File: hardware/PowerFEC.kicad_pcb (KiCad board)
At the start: 2 copper layers, 24 x 27.9 mm, 27 parts, among them J1 105444-0001, J2 B2B-XH-A, U1 PIC16F1455, U2 AP22652, U3 ZXCT1009

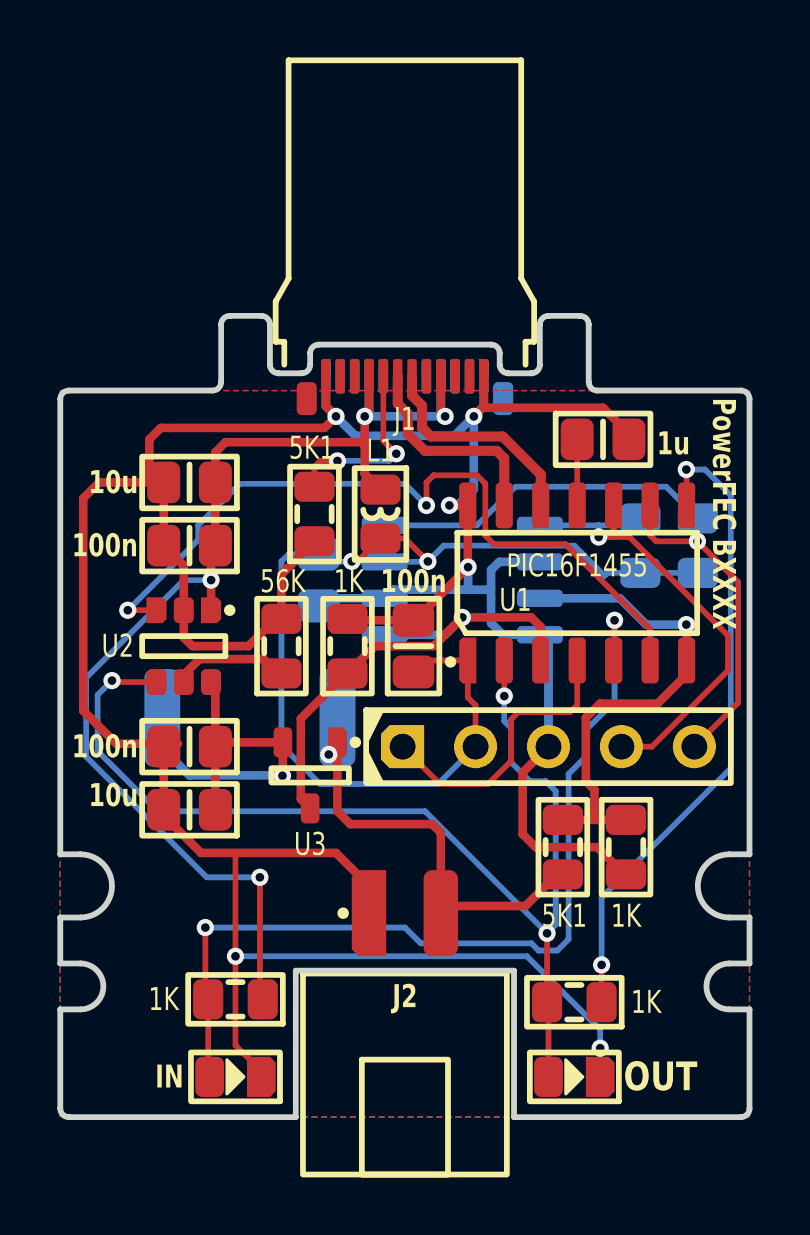
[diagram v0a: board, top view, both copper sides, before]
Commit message: Added 10nF capacitor
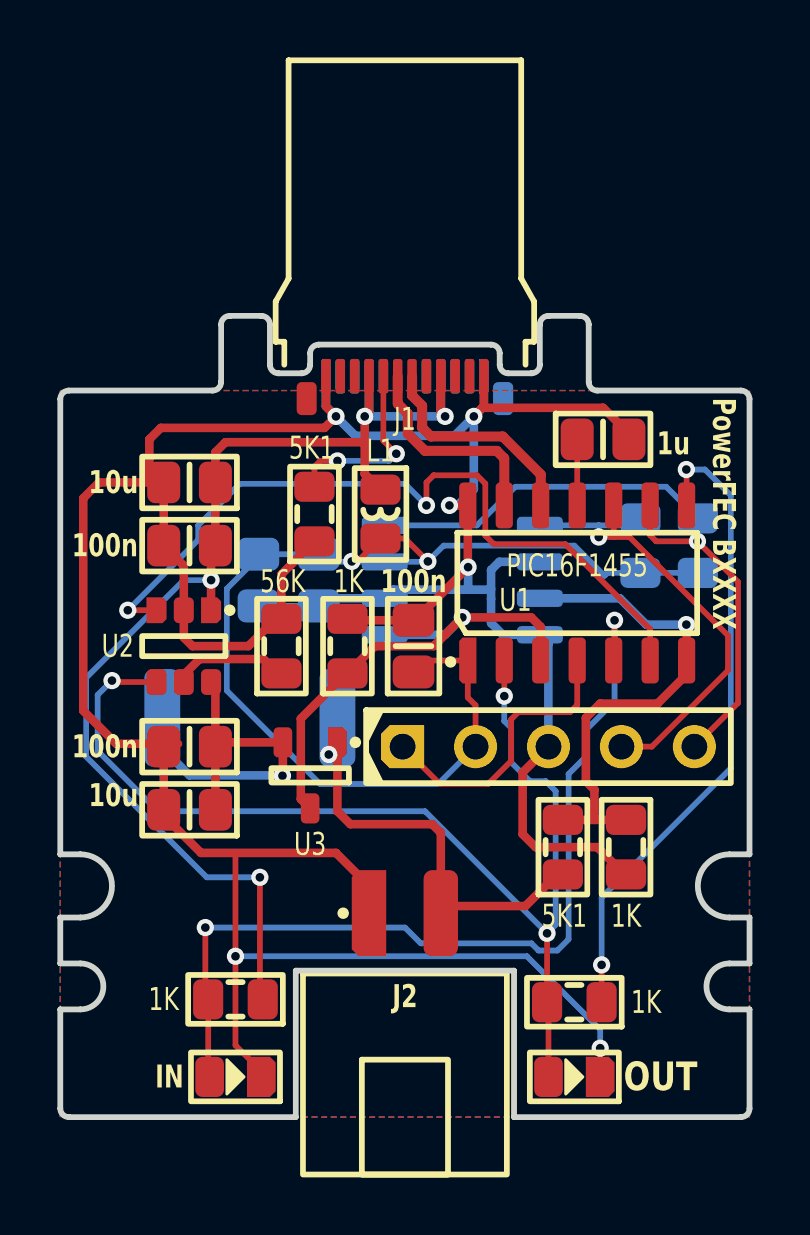
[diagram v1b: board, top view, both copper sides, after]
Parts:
- added C5: 100n, Medo64:C (0805), B.Cu at (26.9, 29.2)
- C1: renamed from C4; value 100n -> 10n
- renumbered C1 to C2, C2 to C3, C3 to C4, C5 to C6, C6 to C7, C7 to C8
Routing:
- net 5V: track 37.4 -> 39.6 mm
- net GND: track 124.7 -> 126.7 mm
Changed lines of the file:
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@@
     (tags "CAPC2013X140N")
     (attr smd)
-    (fp_text reference "C7" (at 0 -1.6) (layer "F.SilkS") hide
+    (fp_text reference "C8" (at 0 -1.6) (layer "F.SilkS") hide
         (effects (font (size 0.8 0.6) (thickness 0.15) bold))
     )
@@
     (tags "CAPC2013X140N")
     (attr smd)
-    (fp_text reference "C6" (at 0 -1.6) (layer "F.SilkS") hide
+    (fp_text reference "C7" (at 0 -1.6) (layer "F.SilkS") hide
         (effects (font (size 0.8 0.6) (thickness 0.15) bold))
     )
@@
     (tags "CAPC2013X140N")
     (attr smd)
-    (fp_text reference "C1" (at 0 -1.6) (layer "F.SilkS") hide
+    (fp_text reference "C2" (at 0 -1.6) (layer "F.SilkS") hide
         (effects (font (size 0.8 0.6) (thickness 0.15) bold))
     )
@@
     (tags "CAPC2013X140N")
     (attr smd)
-    (fp_text reference "C2" (at 0 -1.6) (layer "F.SilkS") hide
+    (fp_text reference "C3" (at 0 -1.6) (layer "F.SilkS") hide
         (effects (font (size 0.8 0.6) (thickness 0.15) bold))
     )
@@
     (tags "CAPC2013X140N")
     (attr smd)
-    (fp_text reference "C5" (at 0 -1.6) (layer "F.SilkS") hide
+    (fp_text reference "C6" (at 0 -1.6) (layer "F.SilkS") hide
         (effects (font (size 0.8 0.6) (thickness 0.15) bold))
     )
@@
     (tags "CAPC2013X140N")
     (attr smd)
-    (fp_text reference "C3" (at 0 -1.6 90) (layer "F.SilkS") hide
+    (fp_text reference "C4" (at 0 -1.6 90) (layer "F.SilkS") hide
         (effects (font (size 0.8 0.6) (thickness 0.15) bold))
     )
@@
     (tags "CAPC2013X140N")
     (attr smd)
-    (fp_text reference "C4" (at 0 1.6 90) (layer "B.SilkS") hide
+    (fp_text reference "C1" (at 0 1.6 90) (layer "B.SilkS") hide
         (effects (font (size 0.8 0.6) (thickness 0.15) bold) (justify mirror))
     )
-    (fp_text value "100n" (at 2.25 0) (layer "B.SilkS")
+    (fp_text value "10n" (at 2.25 0) (layer "B.SilkS")
         (effects (font (size 0.8 0.6) (thickness 0.15) bold) (justify mirror))
     )
@@
       (net 4 "GND") (thermal_bridge_angle 45))
     (model ":KICAD7_3DMODEL_DIR:Package_SO.3dshapes/SO-8_3.9x4.9mm_P1.27mm.step"
+      (offset (xyz 0 0 0))
+      (scale (xyz 1 1 1))
+      (rotate (xyz 0 0 0))
+    )
+  )
+  (footprint "Medo64:C (0805)" (layer "B.Cu")
+    (at 26.9 29.2 -90)
+    (tags "CAPC2013X140N")
+    (attr smd)
+    (fp_text reference "C5" (at 0 1.6 90) (layer "B.SilkS") hide
+        (effects (font (size 0.8 0.6) (thickness 0.15) bold) (justify mirror))
+    )
+    (fp_text value "100n" (at 2.25 0) (layer "B.SilkS")
+        (effects (font (size 0.8 0.6) (thickness 0.15) bold) (justify mirror))
+    )
+    (fp_line (start 0 0.625) (end 0 -0.625)
+      (stroke (width 0.2) (type default)) (layer "B.SilkS"))
+    (fp_rect (start -1.65 0.9) (end 1.65 -0.9)
+      (stroke (width 0.2) (type default)) (fill none) (layer "B.SilkS"))
+    (fp_rect (start -1.75 1) (end 1.75 -1)
+      (stroke (width 0.01) (type dash)) (fill none) (layer "B.CrtYd"))
+    (fp_rect (start -1 0.625) (end 1 -0.625)
+      (stroke (width 0.01) (type dash_dot)) (fill none) (layer "B.Fab"))
+    (pad "1" smd roundrect (at -0.9 0 270) (size 1.15 1.45) (layers "B.Cu" "B.Paste" "B.Mask") (roundrect_rratio 0.25)
+      (net 8 "5V") (thermal_bridge_angle 45))
+    (pad "2" smd roundrect (at 0.9 0 270) (size 1.15 1.45) (layers "B.Cu" "B.Paste" "B.Mask") (roundrect_rratio 0.25)
+      (net 4 "GND") (thermal_bridge_angle 45))
+    (model ":KICAD7_3DMODEL_DIR:Capacitor_SMD.3dshapes/C_0805_2012Metric.step"
       (offset (xyz 0 0 0))
       (scale (xyz 1 1 1))
@@
   (segment (start 35.41 31.105) (end 36.7 31.105) (width 0.3) (layer "B.Cu") (net 4))
   (segment (start 37 31.405) (end 37 35) (width 0.3) (layer "B.Cu") (net 4))
+  (segment (start 29 30.1) (end 27 30.1) (width 0.2) (layer "B.Cu") (net 4))
   (segment (start 34.2 28.75) (end 34.200002 28.750002) (width 0.3) (layer "B.Cu") (net 4))
   (segment (start 31.3 29.835) (end 29.265 29.835) (width 0.3) (layer "B.Cu") (net 4))
@@
   (via (at 32.8 28.55) (size 0.6) (drill 0.3) (layers "F.Cu" "B.Cu") (net 8))
   (via (at 30.15 28.55) (size 0.6) (drill 0.3) (layers "F.Cu" "B.Cu") (net 8))
-  (segment (start 27.7 34.95) (end 27.7 28.55) (width 0.2) (layer "B.Cu") (net 8))
-  (segment (start 27.95 28.3) (end 29 28.3) (width 0.2) (layer "B.Cu") (net 8))
+  (segment (start 25.8 29.5) (end 25.8 33.05) (width 0.2) (layer "B.Cu") (net 8))
+  (segment (start 27 28.3) (end 25.8 29.5) (width 0.2) (layer "B.Cu") (net 8))
   (segment (start 40.2 28.95) (end 42.2 28.95) (width 0.2) (layer "B.Cu") (net 8))
-  (segment (start 27.7 28.55) (end 27.95 28.3) (width 0.2) (layer "B.Cu") (net 8))
-  (segment (start 33.16 36.3) (end 29.05 36.3) (width 0.2) (layer "B.Cu") (net 8))
+  (segment (start 25.8 33.05) (end 29.05 36.3) (width 0.2) (layer "B.Cu") (net 8))
+  (segment (start 33.16 36.3) (end 34.46 35) (width 0.2) (layer "B.Cu") (net 8))
   (segment (start 31.3 28.565) (end 32.785 28.565) (width 0.2) (layer "B.Cu") (net 8))
   (segment (start 39.05 28.95) (end 38.95 29.05) (width 0.2) (layer "B.Cu") (net 8))
   (segment (start 32.785 28.565) (end 32.8 28.55) (width 0.2) (layer "B.Cu") (net 8))
-  (segment (start 34.46 35) (end 33.16 36.3) (width 0.2) (layer "B.Cu") (net 8))
-  (segment (start 29.05 36.3) (end 27.7 34.95) (width 0.2) (layer "B.Cu") (net 8))
+  (segment (start 29 28.3) (end 27 28.3) (width 0.2) (layer "B.Cu") (net 8))
   (segment (start 40.2 28.95) (end 39.05 28.95) (width 0.2) (layer "B.Cu") (net 8))
   (segment (start 31.3 28.565) (end 29.265 28.565) (width 0.2) (layer "B.Cu") (net 8))
   (segment (start 37.9 28) (end 33.35 28) (width 0.2) (layer "B.Cu") (net 8))
+  (segment (start 29.05 36.3) (end 33.16 36.3) (width 0.2) (layer "B.Cu") (net 8))
   (segment (start 33.35 28) (end 32.8 28.55) (width 0.2) (layer "B.Cu") (net 8))
   (segment (start 38.95 29.05) (end 37.9 28) (width 0.2) (layer "B.Cu") (net 8))

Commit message: Replaced current sense resistor with smaller one
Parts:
- R1: footprint Medo64:R (2512) -> Medo64:R (1206)
- moved R1 1.63 mm to (28.2, 33.7)
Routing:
- net Vsw: track 12.3 -> 8.51 mm
- net Vout: track 14.1 -> 15.5 mm
- net 5V: track 39.6 -> 40.7 mm
- net GND: track 126.7 -> 126.9 mm, vias 6 -> 7
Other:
- board text added: "PowerFEC CXXXX"
- board text removed: "PowerFEC BXXXX"

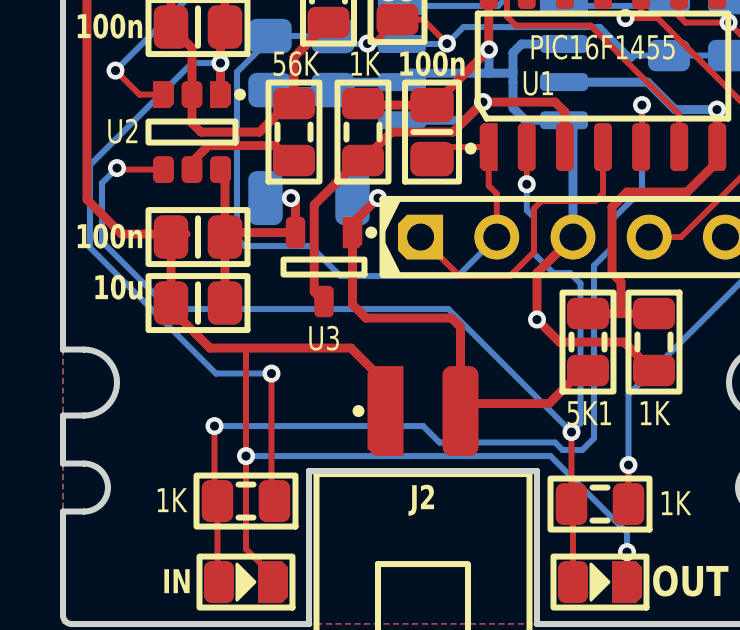
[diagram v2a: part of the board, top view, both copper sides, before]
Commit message: Added output labels
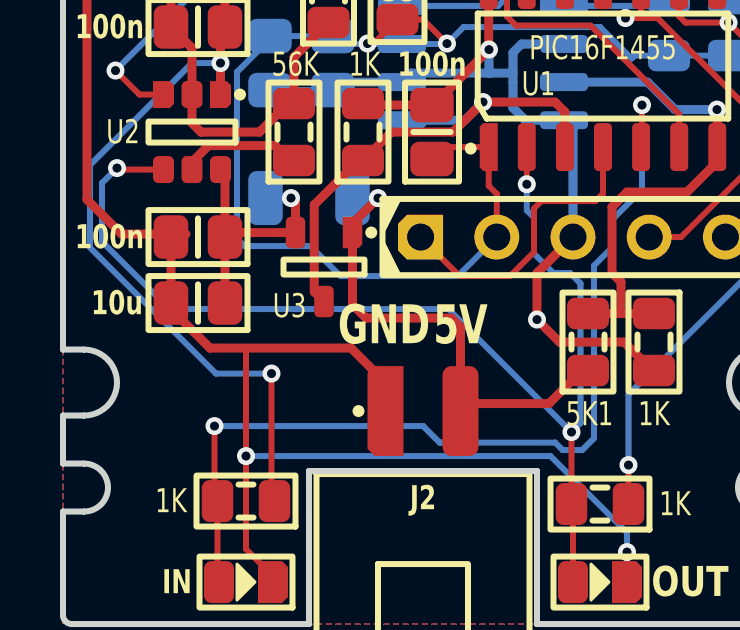
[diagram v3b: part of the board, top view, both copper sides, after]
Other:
- board text added: "5V"
- board text added: "GND"
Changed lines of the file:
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@@
         (effects (font (size 0.8 0.6) (thickness 0.15) bold))
     )
-    (fp_text value "10u" (at 2.65 0.5) (layer "F.SilkS")
+    (fp_text value "10u" (at 2.7 0) (layer "F.SilkS")
         (effects (font (size 0.8 0.6) (thickness 0.15) bold))
     )
@@
     (tags "SOT95P240X110-3N")
     (attr smd)
-    (fp_text reference "U3" (at 0 -2.4 180) (layer "F.SilkS")
+    (fp_text reference "U3" (at 1.15 -1.3 180) (layer "F.SilkS")
         (effects (font (size 0.8 0.6) (thickness 0.15)))
     )
@@
   (gr_circle locked (center 20.7 39.85) (end 23.15 39.85)
     (stroke (width 0.01) (type solid)) (fill none) (layer "Margin"))
+  (gr_text "5V" (at 33.25 38.7) (layer "F.SilkS" knockout)
+    (effects (font (size 1.3 0.9) (thickness 0.15) bold) (justify bottom))
+  )
+  (gr_text "GND" (at 30.7 38.7) (layer "F.SilkS" knockout)
+    (effects (font (size 1.3 0.9) (thickness 0.15) bold) (justify bottom))
+  )
   (gr_text "PowerFEC CXXXX" (at 43.1 22.85 270) (layer "F.SilkS")
     (effects (font (size 0.8 0.6) (thickness 0.15) bold) (justify left))
@@
     (connect_pads no (clearance 0.3))
     (min_thickness 0.3) (filled_areas_thickness no)
-    (fill yes (thermal_gap 0.5) (thermal_bridge_width 0.5))
+    (fill (thermal_gap 0.5) (thermal_bridge_width 0.5))
     (polygon
       (pts

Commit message: Refactoring a bit
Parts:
- U2: footprint Medo64:U LoadSwitch Adjustable LatchOff EnableLow [AP22652AW6-7] (SOT23-6) -> Medo64:U LoadSwitch Adjustable [AP22652AW6-7] (SOT23-6)
- gave numbers to parts that had none: 1
